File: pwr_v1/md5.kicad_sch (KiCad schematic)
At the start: 17 parts, among them M5 Conn_01x08_Socket

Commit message: Schematic and layout updated
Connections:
- net GNDREF: no longer 5C6.2, 5U1.4 (GND_BK), M5.4 (Pin_4)
- new net GND_BK: 5C6.2, 5U1.4 (GND_BK), M5.4 (Pin_4)
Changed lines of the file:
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@@
-	)
-	(junction
-		(at 132.334 50.419)
-		(diameter 0)
-		(color 0 0 0 0)
 	)
 	(junction
@@
 	)
 	(junction
-		(at 119.634 50.419)
-		(diameter 0)
-		(color 0 0 0 0)
-	)
-	(junction
 		(at 190.754 85.09)
 		(diameter 0)
@@
 	)
 	(junction
-		(at 198.374 69.85)
-		(diameter 0)
-		(color 0 0 0 0)
-	)
-	(junction
 		(at 190.754 92.71)
 		(diameter 0)
@@
 	(wire
 		(pts
-			(xy 198.374 50.419) (xy 132.334 50.419)
-		)
-		(stroke
-			(width 0)
-			(type default)
-		)
-	)
-	(wire
-		(pts
-			(xy 190.754 92.71) (xy 190.754 93.98)
-		)
-		(stroke
-			(width 0)
-			(type default)
-		)
-	)
-	(wire
-		(pts
 			(xy 179.324 92.71) (xy 190.754 92.71)
 		)
@@
 	(wire
 		(pts
-			(xy 114.3 50.419) (xy 119.634 50.419)
-		)
-		(stroke
-			(width 0)
-			(type default)
-		)
-	)
-	(wire
-		(pts
 			(xy 218.694 114.3) (xy 244.094 114.3)
 		)
@@
 	(wire
 		(pts
+			(xy 119.634 50.419) (xy 119.634 57.15)
+		)
+		(stroke
+			(width 0)
+			(type default)
+		)
+	)
+	(wire
+		(pts
 			(xy 186.944 85.09) (xy 190.754 85.09)
 		)
@@
 	(wire
 		(pts
-			(xy 198.374 50.419) (xy 198.374 69.85)
-		)
-		(stroke
-			(width 0)
-			(type default)
-		)
-	)
-	(wire
-		(pts
 			(xy 178.054 55.88) (xy 188.214 55.88)
 		)
@@
 		(pts
 			(xy 138.684 111.76) (xy 138.684 120.65)
-		)
-		(stroke
-			(width 0)
-			(type default)
-		)
-	)
-	(wire
-		(pts
-			(xy 119.634 50.419) (xy 119.634 57.15)
 		)
 		(stroke
@@
 	(text "AVDD 3.3V/30mA"
 		(exclude_from_sim no)
-		(at 176.403 50.165 0)
+		(at 199.136 71.12 0)
 		(effects
 			(font
@@
 	)
 	(label "AVDD"
-		(at 114.3 50.419 0)
+		(at 119.634 50.546 0)
 		(fields_autoplaced yes)
 		(effects
@@
 					(unit 1)
 				)
-			)
-		)
-	)
-	(symbol
-		(lib_id "power:GNDREF")
-		(at 190.754 93.98 0)
-		(unit 1)
-		(exclude_from_sim no)
-		(in_bom yes)
-		(on_board yes)
-		(dnp no)
-		(property "Reference" "#PWR047"
-			(at 190.754 100.33 0)
-			(effects
-				(font
-					(size 1.27 1.27)
-				)
-				(hide yes)
-			)
-		)
-		(property "Value" "GNDREF"
-			(at 190.754 97.79 0)
-			(effects
-				(font
-					(size 1.27 1.27)
-				)
-				(hide yes)
-			)
-		)
-		(property "Footprint" ""
-			(at 190.754 93.98 0)
-			(effects
-				(font
-					(size 1.27 1.27)
-				)
-				(hide yes)
-			)
-		)
-		(property "Datasheet" ""
-			(at 190.754 93.98 0)
-			(effects
-				(font
-					(size 1.27 1.27)
-				)
-				(hide yes)
-			)
-		)
-		(property "Description" ""
-			(at 190.754 93.98 0)
-			(effects
-				(font
-					(size 1.27 1.27)
-				)
-				(hide yes)
-			)
-		)
-		(pin "1"
-		)
-		(instances
-			(project "pwr_v1"
-				(path "/42eee4f9-ea65-4e89-8296-df9554a24009/21707740-0477-4ca7-a08b-de3269a77e6b"
-					(reference "#PWR047")
-					(unit 1)
-				)

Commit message: Schematic updated
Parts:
- 5C1: footprint Capacitor_SMD:C_0805_2012Metric -> Capacitor_SMD:C_0402_1005Metric
- 5C2, 5C4, 5C6: footprint Capacitor_SMD:C_0603_1608Metric -> Capacitor_SMD:C_0402_1005Metric
- 5R1: footprint Resistor_SMD:R_0603_1608Metric_Pad0.98x0.95mm_HandSolder -> Resistor_SMD:R_0603_1608Metric

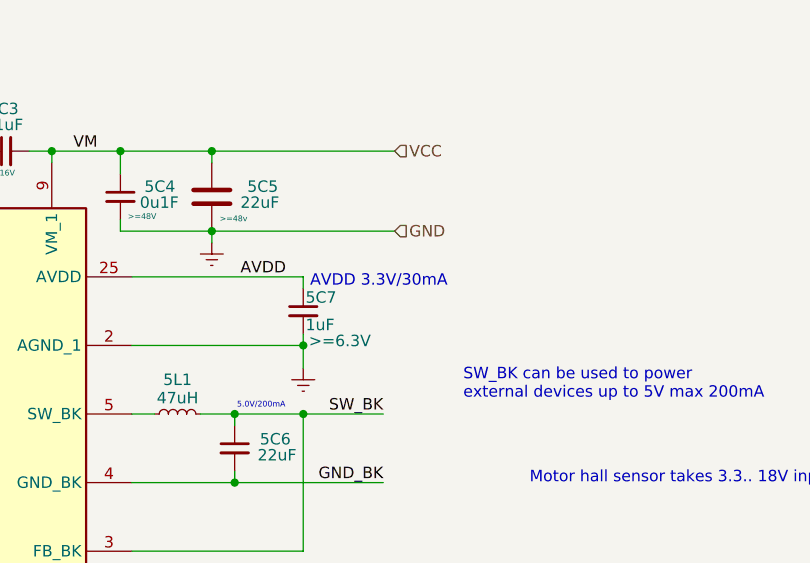
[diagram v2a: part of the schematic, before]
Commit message: Sch and Layout updated; Added batt sup ckt, placed and routed all motor drivers.
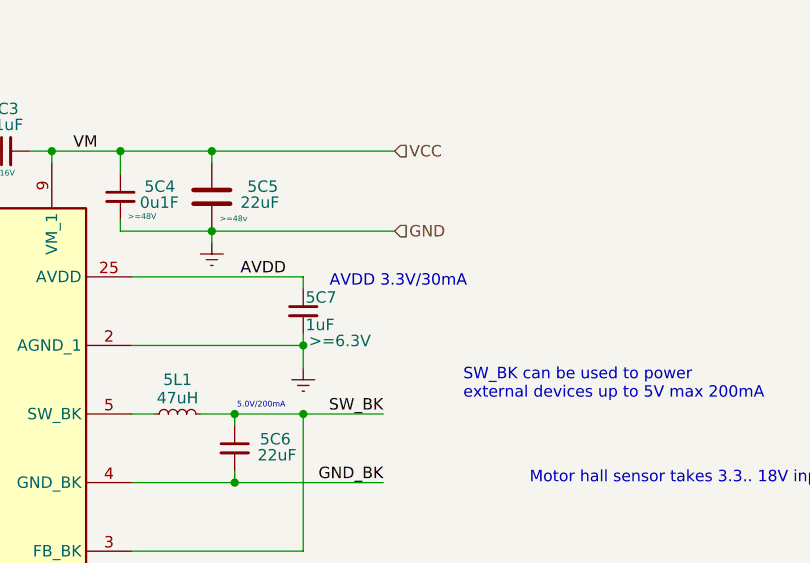
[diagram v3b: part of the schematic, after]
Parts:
- M5: footprint Connector_PinHeader_2.54mm:PinHeader_1x08_P2.54mm_Vertical_SMD_Pin1Left -> Connector_PinHeader_2.54mm:PinHeader_1x08_P2.54mm_Vertical
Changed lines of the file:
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@@
 	(text "AVDD 3.3V/30mA"
 		(exclude_from_sim no)
-		(at 199.136 71.12 0)
+		(at 201.295 71.12 0)
 		(effects
 			(font
@@
 			)
 		)
-		(property "Footprint" "Connector_PinHeader_2.54mm:PinHeader_1x08_P2.54mm_Vertical_SMD_Pin1Left"
+		(property "Footprint" "Connector_PinHeader_2.54mm:PinHeader_1x08_P2.54mm_Vertical"
 			(at 249.174 111.76 0)
 			(effects

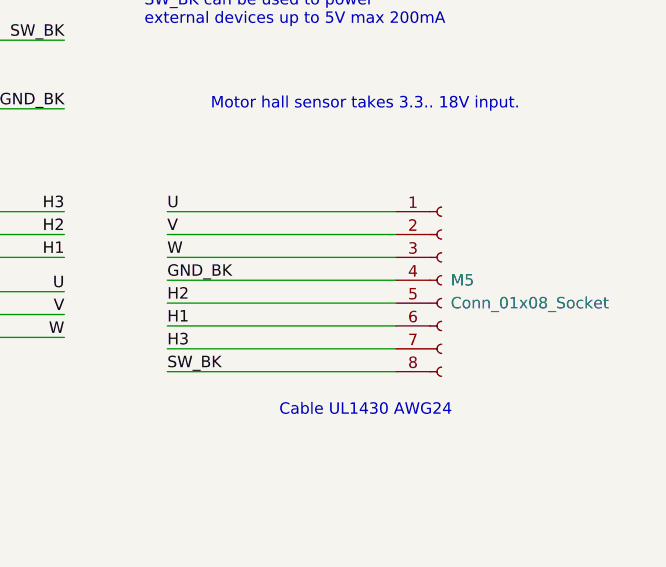
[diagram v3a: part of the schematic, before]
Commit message: Schematic and layout updated; Motor driver alignments and planes;  Few components updated
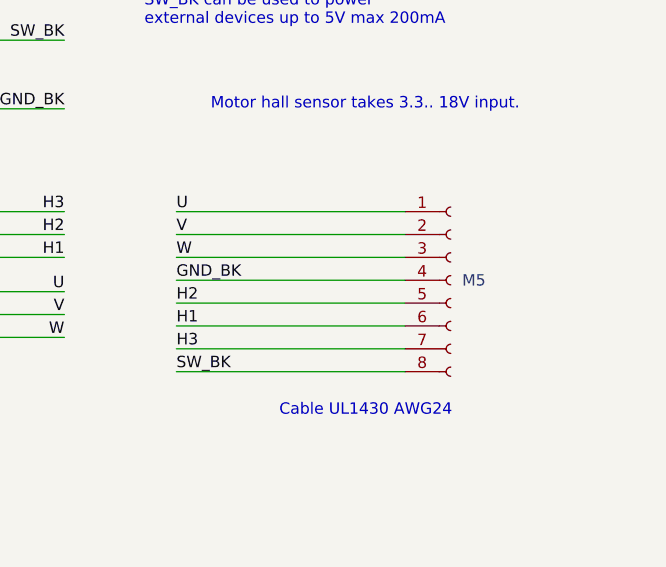
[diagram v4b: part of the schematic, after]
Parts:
- M5: footprint Connector_PinHeader_2.54mm:PinHeader_1x08_P2.54mm_Vertical -> Connector_Molex:Molex_KK-254_AE-6410-08A_1x08_P2.54mm_Vertical
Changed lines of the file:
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@@
 	(wire
 		(pts
-			(xy 218.694 119.38) (xy 244.094 119.38)
+			(xy 219.71 119.38) (xy 245.11 119.38)
 		)
 		(stroke
@@
 	(wire
 		(pts
-			(xy 218.694 109.22) (xy 244.094 109.22)
+			(xy 219.71 109.22) (xy 245.11 109.22)
 		)
 		(stroke
@@
 	(wire
 		(pts
-			(xy 218.694 111.76) (xy 244.094 111.76)
+			(xy 219.71 111.76) (xy 245.11 111.76)
 		)
 		(stroke
@@
 	(wire
 		(pts
-			(xy 218.694 106.68) (xy 244.094 106.68)
+			(xy 219.71 106.68) (xy 245.11 106.68)
 		)
 		(stroke
@@
 	(wire
 		(pts
-			(xy 218.694 114.3) (xy 244.094 114.3)
+			(xy 219.71 114.3) (xy 245.11 114.3)
 		)
 		(stroke
@@
 	(wire
 		(pts
-			(xy 218.694 121.92) (xy 244.094 121.92)
+			(xy 219.71 121.92) (xy 245.11 121.92)
 		)
 		(stroke
@@
 	(wire
 		(pts
-			(xy 218.694 116.84) (xy 244.094 116.84)
+			(xy 219.71 116.84) (xy 245.11 116.84)
 		)
 		(stroke
@@
 	(wire
 		(pts
-			(xy 218.694 104.14) (xy 244.094 104.14)
+			(xy 219.71 104.14) (xy 245.11 104.14)
 		)
 		(stroke
@@
 	)
 	(label "H1"
-		(at 218.694 116.84 0)
+		(at 219.71 116.84 0)
 		(fields_autoplaced yes)
 		(effects
@@
 	)
 	(label "H3"
-		(at 218.694 119.38 0)
+		(at 219.71 119.38 0)
 		(fields_autoplaced yes)
 		(effects
@@
 	)
 	(label "U"
-		(at 218.694 104.14 0)
+		(at 219.71 104.14 0)
 		(fields_autoplaced yes)
 		(effects
@@
 	)
 	(label "SW_BK"
-		(at 218.694 121.92 0)
+		(at 219.71 121.92 0)
 		(fields_autoplaced yes)
 		(effects
@@
 	)
 	(label "W"
-		(at 218.694 109.22 0)
+		(at 219.71 109.22 0)
 		(fields_autoplaced yes)
 		(effects
@@
 	)
 	(label "GND_BK"
-		(at 218.694 111.76 0)
+		(at 219.71 111.76 0)
 		(fields_autoplaced yes)
 		(effects
@@
 	)
 	(label "V"
-		(at 218.694 106.68 0)
+		(at 219.71 106.68 0)
 		(fields_autoplaced yes)
 		(effects
@@
 	)
 	(label "H2"
-		(at 218.694 114.3 0)
+		(at 219.71 114.3 0)
 		(fields_autoplaced yes)
 		(effects
@@
 	(symbol
 		(lib_id "Connector:Conn_01x08_Socket")
-		(at 249.174 111.76 0)
+		(at 250.19 111.76 0)
 		(unit 1)
 		(exclude_from_sim no)
@@
 		(fields_autoplaced yes)
 		(property "Reference" "M5"
-			(at 250.19 111.7599 0)
+			(at 251.46 111.7599 0)
 			(effects
 				(font
@@
 		)
 		(property "Value" "Conn_01x08_Socket"
-			(at 250.19 114.2999 0)
-			(effects
-				(font
-					(size 1.27 1.27)
-				)
-				(justify left)
-			)
-		)
-		(property "Footprint" "Connector_PinHeader_2.54mm:PinHeader_1x08_P2.54mm_Vertical"
-			(at 249.174 111.76 0)
+			(at 251.46 114.2999 0)
+			(effects
+				(font
+					(size 1.27 1.27)
+				)
+				(justify left)
+				(hide yes)
+			)
+		)
+		(property "Footprint" "Connector_Molex:Molex_KK-254_AE-6410-08A_1x08_P2.54mm_Vertical"
+			(at 250.19 111.76 0)
 			(effects
 				(font
@@
 		)
 		(property "Datasheet" "~"
-			(at 249.174 111.76 0)
-			(effects
-				(font
-					(size 1.27 1.27)
-				)
-				(hide yes)
-			)
-		)
-		(property "Description" "MFR.Part # X6511WVS-08H-C60D48R2 JLCPCB Part # C2883765"
-			(at 249.174 111.76 0)
-			(effects
-				(font
+			(at 250.19 111.76 0)
+			(effects
+				(font
+					(size 1.27 1.27)
+				)
+				(hide yes)
+			)
+		)
+		(property "Description" ""
+			(at 250.19 111.76 0)
+			(effects
+				(font

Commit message: Schematic and layout updated; Layout placement and routing completed
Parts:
- M5: footprint Connector_Molex:Molex_KK-254_AE-6410-08A_1x08_P2.54mm_Vertical -> Connector_PinHeader_2.54mm:PinHeader_1x08_P2.54mm_Vertical

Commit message: Sch: 0ohm res added to SPI pins, MD footprints updated; Lay: Silkscreen aligned, logo added, DRC
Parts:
- 5U1: footprint MTR:RGF0040E-IPC_B -> motorDriver:RGF0040E-IPC_B
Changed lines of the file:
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@@
 			)
 		)
-		(property "Footprint" "MTR:RGF0040E-IPC_B"
+		(property "Footprint" "motorDriver:RGF0040E-IPC_B"
 			(at 221.234 62.23 0)
 			(effects

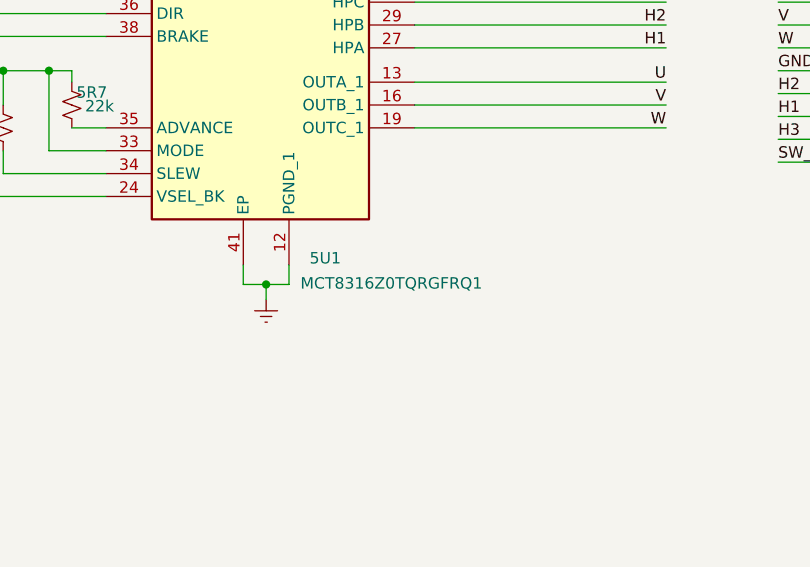
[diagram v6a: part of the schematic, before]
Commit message: Sch: DNP updated, JLC part numbers updated for all components; Lay: Fiducial placement, routing aligned.
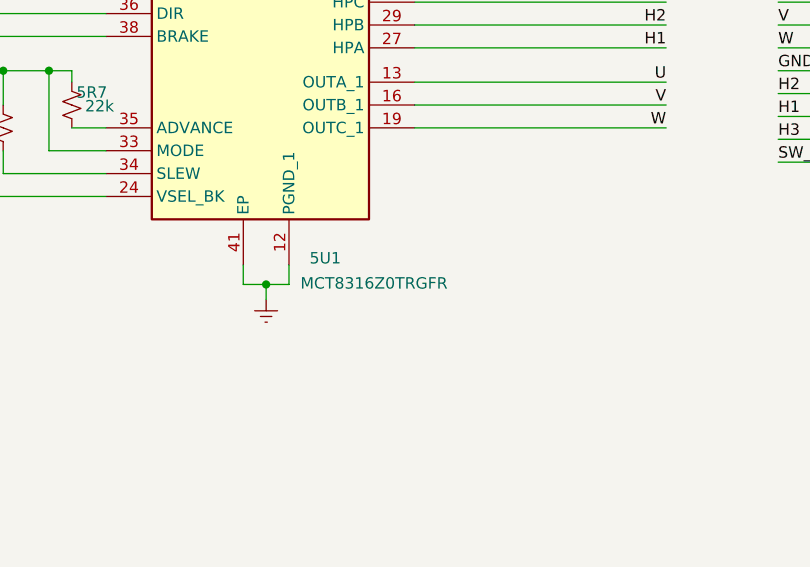
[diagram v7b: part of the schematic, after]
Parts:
- 5U1: value MCT8316Z0TQRGFRQ1 -> MCT8316Z0TRGFR
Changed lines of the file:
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@@
 			)
 		)
-		(property "Description" "Resistor, small US symbol"
+		(property "Description" "MFR.Part # 0603WAF2002T5E JLCPCB Part # C4184"
 			(at 132.334 73.66 0)
 			(effects
@@
 			)
 		)
-		(property "Description" "Resistor, small US symbol"
+		(property "Description" "MFR.Part # 0603WAF2702T5E JLCPCB Part # C22967"
 			(at 132.334 59.69 0)
 			(effects
@@
 			)
 		)
-		(property "Description" "Resistor, small US symbol"
+		(property "Description" "MFR.Part # 0402WGF4702TCE JLCPCB Part # C25792"
 			(at 133.604 118.11 0)
 			(effects
@@
 			)
 		)
-		(property "Description" "Resistor, small US symbol"
+		(property "Description" "MFR.Part # RC0805FR-071ML JLCPCB Part # C107700"
 			(at 127.254 118.11 0)
 			(effects
@@
 			)
 		)
-		(property "Value" "MCT8316Z0TQRGFRQ1"
+		(property "Value" "MCT8316Z0TRGFR"
 			(at 166.624 135.382 0)
 			(effects
@@
 			)
 		)
-		(property "Description" ""
+		(property "Description" "MFR.Part # MCT8316Z0TRGFR JLCPCB Part # C3681342"
 			(at 145.034 74.93 0)
 			(effects
@@
 			)
 		)
-		(property "Description" "Resistor, small US symbol"
+		(property "Description" "MFR.Part # 0402WGJ0223TCE JLCPCB Part # C25547"
 			(at 141.224 115.57 0)
 			(effects
@@
 			)
 		)
-		(property "Description" ""
+		(property "Description" "MFR.Part # HB-PH3-25418PB2GOP JLCPCB Part # C6332201"
 			(at 250.19 111.76 0)
 			(effects

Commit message: Final PCB files sent for fab
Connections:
- net GNDREF renamed GND
